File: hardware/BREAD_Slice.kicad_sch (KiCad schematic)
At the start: 15 parts, among them J1 Conn_01x10_Female, J2 I2C_01x04

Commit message: Initial commit
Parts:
- added C5, C6: 0.01 uF, Capacitor_SMD:C_1206_3216Metric, symbol Device:C
- added D2, D3: General_Purpose_Diode, Diode_THT:D_DO-35_SOD27_P7.62mm_Horizontal, symbol OCI_UPL_4_Semiconductors:General_Purpose_Diode
- added F1, F2: 10A, SparkFun-Fuse:Glass Fuse Clip 5x20MM, symbol OCI_UPL_11_Mechanical:FUSE_Blade
- added FB1, FB2, FB3, FB4: Ferrite_Bead_Small, Resistor_SMD:R_1206_3216Metric, symbol Device:Ferrite_Bead_Small
- added J10, J13, J14, J15, J16, J17, J18, J6, J7, J8, J9: Term_PressFit_Phoenix_Contact, SparkFun-Connector:Term_PressFit_5mm_H_PC_HVRELAY, symbol SparkFun-Connector:Term_PressFit_Phoenix_Contact
- added J11, J12, J3: Term_PressFit_Phoenix_Contact, SparkFun-Connector:Term_PressFit_3.5mm_H_PC, symbol SparkFun-Connector:Term_PressFit_Phoenix_Contact
- added J4: Term_PressFit_Phoenix_Contact, SparkFun-Connector:Term_PressFit_3.5mm_H_ENDCAP_PC, symbol SparkFun-Connector:Term_PressFit_Phoenix_Contact
- added J5: Term_PressFit_Phoenix_Contact, SparkFun-Connector:Term_PressFit_5mm_H_ENDCAP_PC_HVRELAY, symbol SparkFun-Connector:Term_PressFit_Phoenix_Contact
- added K1, K2: G5Q-1, Relay_THT:Relay_SPDT_Omron-G5Q-1, symbol Relay:G5Q-1
- added U2, U5: TCMT1100, Package_SO:SOP-4_4.4x2.6mm_P1.27mm, symbol Isolator:TCMT1100
- added U3, U4: MAX6675ISA+, MAX6675ISA_:SOIC127P600X175-8N, symbol MAX6675ISA_:MAX6675ISA+
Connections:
- net +12V: now also D2.1 (K), D3.1 (K), K1.5, K2.5
- net +5V: now also U3.4 (VCC), U4.4 (VCC)
- net GND: now also C5.2, C6.2, FB2.1, FB4.1, J16.1, J8.1, U2.2, U2.3, U3.1 (GND), U3.2 (T-), U4.1 (GND), U4.2 (T-), U5.2, U5.3
- net Relay2: now reaches A1.10 (D7)
- net Relay2: now also U5.1
- net SS1: now reaches A1.13 (D10)
- net SS1: now also U3.6 (~{CS})
- net SS2: now reaches A1.14 (D11)
- net SS2: now also U4.6 (~{CS})
- net DATA: now reaches A1.15 (D12)
- net DATA: now also U3.7 (SO), U4.7 (SO)
- net CLK: now reaches A1.16 (D13)
- net CLK: now also U3.5 (SCK), U4.5 (SCK)
- net Relay1: now reaches A1.9 (D6)
- net Relay1: now also U2.1
- new net: FB1.2, J3.1
- new net: FB2.2, J4.1
- new net: FB4.2, J12.1
- new net: D2.2 (A), K1.1, U2.4
- new net: D3.2 (A), K2.1, U5.4
- new net: FB3.2, J11.1
- new net ESTOP1: F2.1, J10.1
- new net ESTOP2: F1.1, J18.1
- new net FUSE1: F2.2, K1.2
- new net FUSE2: F1.2, K2.2
- new net IN1: J7.1, J9.1
- new net IN2: J15.1, J17.1
- new net NC1: J5.1, K1.4
- new net NC2: J13.1, K2.4
- new net NO1: J6.1, K1.3
- new net NO2: J14.1, K2.3
- new net T+1: C5.1, FB1.1, U3.3 (T+)
- new net T+2: C6.1, FB3.1, U4.3 (T+)
- no-connect marks 22 -> 18

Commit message: updated to have new terminals and review
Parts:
- removed C5, C6: 0.01 uF, Capacitor_SMD:C_1206_3216Metric, symbol Device:C
- removed D2, D3: General_Purpose_Diode, Diode_THT:D_DO-35_SOD27_P7.62mm_Horizontal, symbol OCI_UPL_4_Semiconductors:General_Purpose_Diode
- removed FB1, FB2, FB3, FB4: Ferrite_Bead_Small, Resistor_SMD:R_1206_3216Metric, symbol Device:Ferrite_Bead_Small
- removed J10, J13, J14, J15, J16, J17, J18, J6, J7, J8, J9: Term_PressFit_Phoenix_Contact, SparkFun-Connector:Term_PressFit_5mm_H_PC_HVRELAY, symbol SparkFun-Connector:Term_PressFit_Phoenix_Contact
- removed J11, J12, J3: Term_PressFit_Phoenix_Contact, SparkFun-Connector:Term_PressFit_3.5mm_H_PC, symbol SparkFun-Connector:Term_PressFit_Phoenix_Contact
- removed J4: Term_PressFit_Phoenix_Contact, SparkFun-Connector:Term_PressFit_3.5mm_H_ENDCAP_PC, symbol SparkFun-Connector:Term_PressFit_Phoenix_Contact
- removed J5: Term_PressFit_Phoenix_Contact, SparkFun-Connector:Term_PressFit_5mm_H_ENDCAP_PC_HVRELAY, symbol SparkFun-Connector:Term_PressFit_Phoenix_Contact
- removed K1, K2: G5Q-1, Relay_THT:Relay_SPDT_Omron-G5Q-1, symbol Relay:G5Q-1
- removed U2, U5: TCMT1100, Package_SO:SOP-4_4.4x2.6mm_P1.27mm, symbol Isolator:TCMT1100
- removed U3, U4: MAX6675ISA+, MAX6675ISA_:SOIC127P600X175-8N, symbol MAX6675ISA_:MAX6675ISA+
- added J3, J4: Screw_Terminal_01x02, TerminalBlock_Phoenix:TerminalBlock_Phoenix_MPT-0,5-2-2.54_1x02_P2.54mm_Horizontal, symbol Connector:Screw_Terminal_01x02
- added J5, J6: Screw_Terminal_01x06, TerminalBlock_Phoenix:TerminalBlock_Phoenix_MKDS-1,5-6-5.08_1x06_P5.08mm_Horizontal, symbol Connector:Screw_Terminal_01x06
- added SW1, SW2: ESTOP, symbol Switch:SW_Push_Open
- F1, F2: footprint SparkFun-Fuse:Glass Fuse Clip 5x20MM -> Fuse:Fuseholder_Clip-5x20mm_Bel_FC-203-22_Lateral_P17.80x5.00mm_D1.17mm_Horizontal
- HS1: footprint SparkFun-Fuse:Thermal Pad -> KML-Custom:Thermal Pad
- renumbered J2 to J1, J1 to J2
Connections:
- net DATA: now also A1.14 (D11); no longer A1.15 (D12)
- net GND: now also J5.4 (Pin_4), J6.4 (Pin_4)
- net SS2: now also A1.15 (D12); no longer A1.14 (D11)
- net ESTOP1: no longer names the net of F2.1
- net ESTOP1: now also J6.6 (Pin_6), SW2.2 (B)
- net ESTOP2: no longer names the net of F1.1
- net ESTOP2: now also J5.6 (Pin_6), SW1.2 (B)
- net FUSE1 renamed Relay1/IN
- net FUSE2 renamed Relay/IN
- new net: J5.3 (Pin_3), J5.5 (Pin_5), SW1.1 (A)
- new net: J6.3 (Pin_3), J6.5 (Pin_5), SW2.1 (A)
- new net MAX31855K/T+: J3.1 (Pin_1)
- new net MAX31855K/T-: J3.2 (Pin_2)
- new net MAX31855K1/T+: J4.1 (Pin_1)
- new net MAX31855K1/T-: J4.2 (Pin_2)
- new net Relay/NC: J5.1 (Pin_1)
- new net Relay/NO: J5.2 (Pin_2)
- new net Relay1/NC: J6.1 (Pin_1)
- new net Relay1/NO: J6.2 (Pin_2)
- no-connect marks 18 -> 16
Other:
- added sheet MAX31855K (max31855k.kicad_sch)
- added sheet MAX31855K1 (max31855k.kicad_sch)
- added sheet Relay (relay.kicad_sch)
- added sheet Relay1 (relay.kicad_sch)

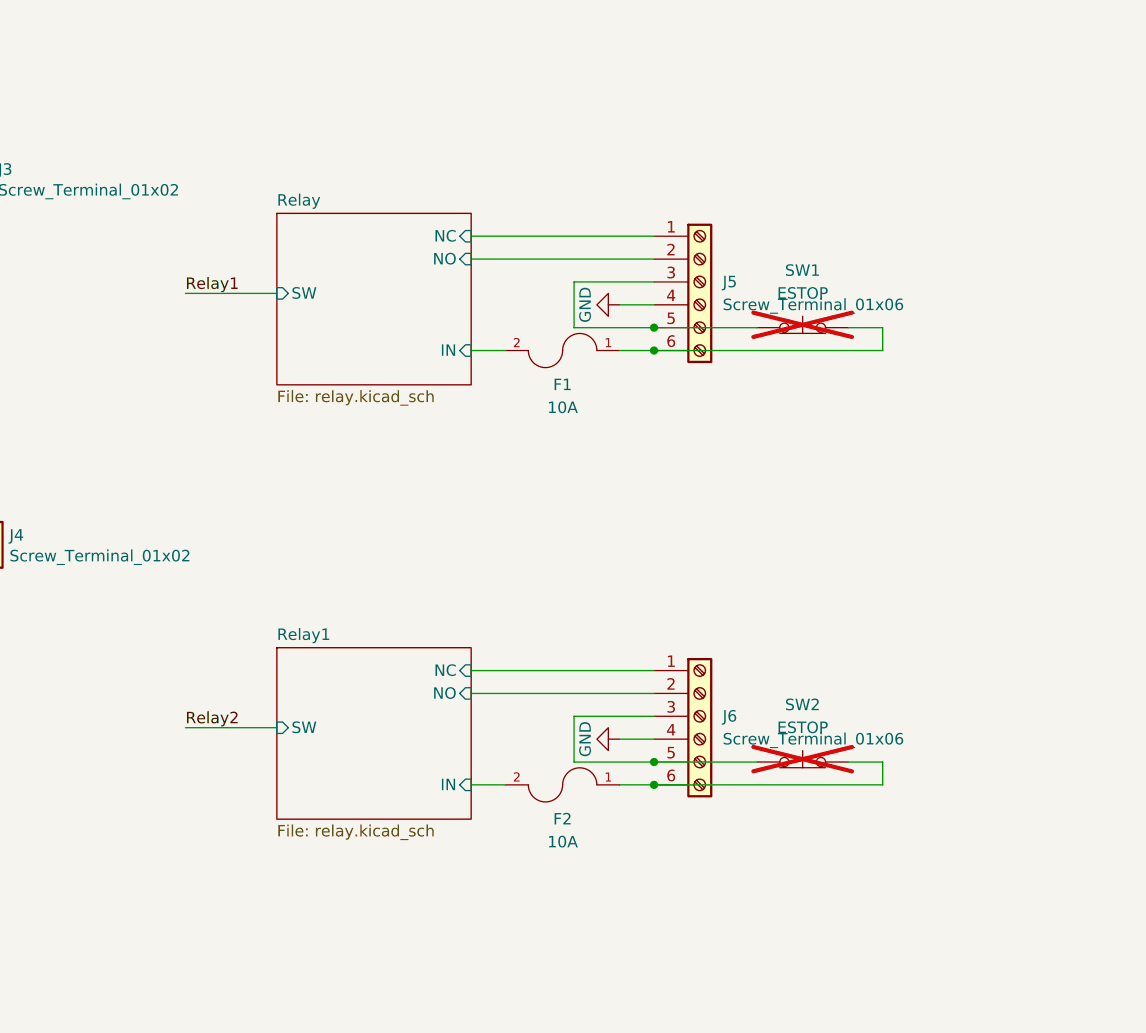
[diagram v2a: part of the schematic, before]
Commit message: updated to have new terminals and review
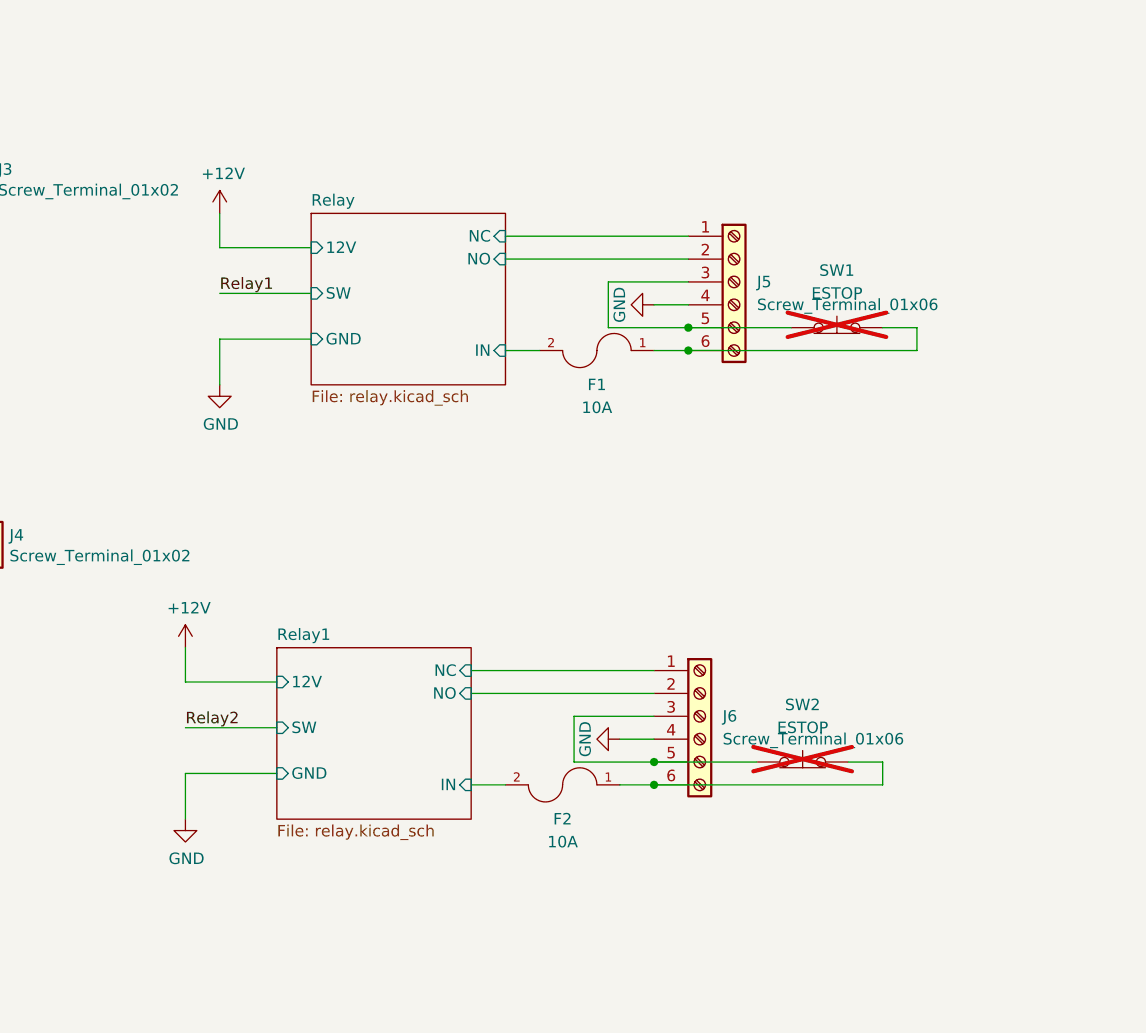
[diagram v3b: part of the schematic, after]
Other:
- sheet Relay ports: added 12V, GND; removed none
- sheet Relay1 ports: added 12V, GND; removed none
- moved on the sheet: F1, J5, SW1
